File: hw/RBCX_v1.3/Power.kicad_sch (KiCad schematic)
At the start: 42 parts

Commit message: Work in progress
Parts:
- removed J? (x3): Conn_02x04_Counter_Clockwise, Connector_PinHeader_2.54mm:PinHeader_2x04_P2.54mm_Vertical, symbol Connector_Generic:Conn_02x04_Counter_Clockwise
- removed LED? (x6): red, LED_SMD:LED_0603_1608Metric, symbol RBCX-eagle-import:LEDCHIPLED_0603
- removed TP? (x2): TP_06MM, RBCX:TP_06MM, symbol RBCX-eagle-import:TP_06MM
- added D27, D28, D29, D30, D31, D32, D47, D48: red, LED_SMD:LED_0603_1608Metric, symbol Device:LED
- added J2, J3, J4: Conn_02x04_Odd_Even, Connector_PinHeader_2.54mm:PinHeader_2x04_P2.54mm_Vertical, symbol Connector_Generic:Conn_02x04_Odd_Even
- added R181, R182: 1k, Resistor_SMD:R_0201_0603Metric, symbol Device:R
- added TP59, TP8: TP_06MM, RBCX:TP_06MM, symbol RBCX-eagle-import:TP_06MM
- gave numbers to parts that had none: 30
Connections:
- net 3V3: now also D31.2 (A), D32.2 (A), D47.2 (A), D48.2 (A), J2.1 (Pin_1), J2.3 (Pin_3), J2.5 (Pin_5), J2.7 (Pin_7), TP59.P$1 (TP)
- net 5V: now also D29.2 (A), D30.2 (A), J3.1 (Pin_1), J3.3 (Pin_3), J3.5 (Pin_5), J3.7 (Pin_7), TP8.P$1 (TP)
- net GND: now also J2.2 (Pin_2), J2.4 (Pin_4), J2.6 (Pin_6), J2.8 (Pin_8), J3.2 (Pin_2), J3.4 (Pin_4), J3.6 (Pin_6), J3.8 (Pin_8), J4.2 (Pin_2), J4.4 (Pin_4), J4.6 (Pin_6), J4.8 (Pin_8), R181.1, R182.1
- net IN: now also D27.2 (A), D28.2 (A), J4.1 (Pin_1), J4.3 (Pin_3), J4.5 (Pin_5), J4.7 (Pin_7)
- net at R14.1: now also D29.1 (K)
- net at R16.2: now also D31.1 (K)
- net at R10.1, R11.1, R9.1: now also U1.4 (FB); no longer U1. (FB)
- net at R13.2: now also D28.1 (K)
- net at R12.2: now also D27.1 (K)
- net at R15.1: now also D30.1 (K)
- net at R17.2: now also D32.1 (K)
- new net: D47.1 (K), R181.2
- new net: D48.1 (K), R182.2
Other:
- moved on the sheet: TP1, TP2

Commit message: New PCB layout
some changes of schema:
- change PD sink AO33772 to AO33771
- remove power switch
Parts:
- J2, J3, J4: footprint Connector_PinHeader_2.54mm:PinHeader_2x04_P2.54mm_Vertical -> RBCX:PinHeader_2x04_P2.54mm_Vertical
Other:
- sheet Battery Manager ports: added CC1, CC2; removed none
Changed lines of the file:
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@@
+    (stroke (width 0) (type default) (color 0 0 0 0))
+  )
+  (wire (pts (xy 170.18 50.8) (xy 170.18 53.34))
     (stroke (width 0) (type default) (color 0 0 0 0))
   )
@@
     (effects (font (size 1.27 1.27)) (justify left))
   )
-  (hierarchical_label "GND" (shape input) (at 69.85 74.93 0)
+  (hierarchical_label "GND" (shape input) (at 69.85 81.28 0)
     (effects (font (size 1.27 1.27)) (justify left))
   )
@@
     (effects (font (size 1.27 1.27)) (justify right))
   )
+  (hierarchical_label "CC1" (shape bidirectional) (at 69.85 74.93 0)
+    (effects (font (size 1.27 1.27)) (justify left))
+  )
   (hierarchical_label "SDA" (shape bidirectional) (at 69.85 64.77 0)
     (effects (font (size 1.27 1.27)) (justify left))
@@
   (hierarchical_label "GND" (shape input) (at 91.44 180.34 270)
     (effects (font (size 1.27 1.27)) (justify right))
+  )
+  (hierarchical_label "CC2" (shape bidirectional) (at 69.85 77.47 0)
+    (effects (font (size 1.27 1.27)) (justify left))
   )
   (hierarchical_label "GND" (shape input) (at 271.78 128.27 270)
@@
     (property "Reference" "J2" (id 0) (at 260.35 88.9 0))
     (property "Value" "Conn_02x04_Odd_Even" (id 1) (at 260.35 91.44 0))
-    (property "Footprint" "Connector_PinHeader_2.54mm:PinHeader_2x04_P2.54mm_Vertical" (id 2) (at 259.08 97.79 0)
+    (property "Footprint" "RBCX:PinHeader_2x04_P2.54mm_Vertical" (id 2) (at 259.08 97.79 0)
       (effects (font (size 1.27 1.27)) hide)
     )
@@
     (pin "2")
   )
+  (symbol (lib_id "power:PWR_FLAG") (at 170.18 50.8 0) (unit 1)
+    (in_bom yes) (on_board yes) (fields_autoplaced)
+    (property "Reference" "#FLG0102" (id 0) (at 170.18 48.895 0)
+      (effects (font (size 1.27 1.27)) hide)
+    )
+    (property "Value" "PWR_FLAG" (id 1) (at 170.18 45.72 0))
+    (property "Footprint" "" (id 2) (at 170.18 50.8 0)
+      (effects (font (size 1.27 1.27)) hide)
+    )
+    (property "Datasheet" "~" (id 3) (at 170.18 50.8 0)
+      (effects (font (size 1.27 1.27)) hide)
+    )
+    (pin "1")
+  )
   (symbol (lib_id "Device:R") (at 73.66 170.18 180) (unit 1)
     (in_bom yes) (on_board yes)
@@
     (property "Reference" "J4" (id 0) (at 260.35 133.35 0))
     (property "Value" "Conn_02x04_Odd_Even" (id 1) (at 260.35 135.89 0))
-    (property "Footprint" "Connector_PinHeader_2.54mm:PinHeader_2x04_P2.54mm_Vertical" (id 2) (at 259.08 142.24 0)
+    (property "Footprint" "RBCX:PinHeader_2x04_P2.54mm_Vertical" (id 2) (at 259.08 142.24 0)
       (effects (font (size 1.27 1.27)) hide)
     )
@@
     (property "Reference" "J3" (id 0) (at 260.35 111.76 0))
     (property "Value" "Conn_02x04_Odd_Even" (id 1) (at 260.35 114.3 0))
-    (property "Footprint" "Connector_PinHeader_2.54mm:PinHeader_2x04_P2.54mm_Vertical" (id 2) (at 259.08 120.65 0)
+    (property "Footprint" "RBCX:PinHeader_2x04_P2.54mm_Vertical" (id 2) (at 259.08 120.65 0)
       (effects (font (size 1.27 1.27)) hide)
     )
@@
     (pin "2")
   )
-  (sheet (at 38.1 38.1) (size 31.75 38.1) (fields_autoplaced)
+  (sheet (at 38.1 38.1) (size 31.75 44.45) (fields_autoplaced)
     (stroke (width 0.1524) (type solid) (color 0 0 0 0))
     (fill (color 0 0 0 0.0000))
@@
       (effects (font (size 1.27 1.27)) (justify left bottom))
     )
-    (property "Sheet file" "Battery_manager.kicad_sch" (id 1) (at 38.1 76.7846 0)
+    (property "Sheet file" "Battery_manager.kicad_sch" (id 1) (at 38.1 83.1346 0)
       (effects (font (size 1.27 1.27)) (justify left top))
     )
-    (pin "GND" input (at 69.85 74.93 0)
+    (pin "GND" input (at 69.85 81.28 0)
       (effects (font (size 1.27 1.27)) (justify right))
     )
@@
       (effects (font (size 1.27 1.27)) (justify right))
     )
+    (pin "CC1" bidirectional (at 69.85 74.93 0)
+      (effects (font (size 1.27 1.27)) (justify right))
+    )
+    (pin "CC2" bidirectional (at 69.85 77.47 0)
+      (effects (font (size 1.27 1.27)) (justify right))
+    )

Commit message: Production files
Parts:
- BAT1: JLCPCB_CORRECTION (none) -> 0;0;180
- J2, J3, J4: JLCPCB_CORRECTION (none) -> 1.27;-3.81;90; LCSC C225289 -> C124386
- TP1, TP2, TP4, TP5, TP59, TP6, TP7, TP8, X1: JLCPCB_IGNORE (none) -> 1
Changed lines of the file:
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@@
       (effects (font (size 1.27 1.27)) hide)
     )
-    (property "LCSC" "C225289" (id 4) (at 259.08 97.79 0)
+    (property "LCSC" "C124386" (id 4) (at 259.08 97.79 0)
       (effects (font (size 1.27 1.27)) hide)
     )
     (property "Basic/Extended" "E" (id 5) (at 259.08 97.79 0)
+      (effects (font (size 1.27 1.27)) hide)
+    )
+    (property "JLCPCB_CORRECTION" "1.27;-3.81;90" (id 6) (at 259.08 97.79 0)
       (effects (font (size 1.27 1.27)) hide)
     )
@@
       (effects (font (size 1.27 1.27)) hide)
     )
+    (property "JLCPCB_IGNORE" "1" (id 4) (at 255.397 35.56 0)
+      (effects (font (size 1.27 1.27)) hide)
+    )
     (pin "P$1")
   )
@@
       (effects (font (size 1.27 1.27)) hide)
     )
-    (property "LCSC" "C225289" (id 4) (at 259.08 142.24 0)
+    (property "LCSC" "C124386" (id 4) (at 259.08 142.24 0)
       (effects (font (size 1.27 1.27)) hide)
     )
     (property "Basic/Extended" "E" (id 5) (at 259.08 142.24 0)
+      (effects (font (size 1.27 1.27)) hide)
+    )
+    (property "JLCPCB_CORRECTION" "1.27;-3.81;90" (id 6) (at 259.08 142.24 0)
       (effects (font (size 1.27 1.27)) hide)
     )
@@
       (effects (font (size 1.27 1.27)) hide)
     )
-    (property "LCSC" "C225289" (id 4) (at 259.08 120.65 0)
+    (property "LCSC" "C124386" (id 4) (at 259.08 120.65 0)
       (effects (font (size 1.27 1.27)) hide)
     )
     (property "Basic/Extended" "E" (id 5) (at 259.08 120.65 0)
+      (effects (font (size 1.27 1.27)) hide)
+    )
+    (property "JLCPCB_CORRECTION" "1.27;-3.81;90" (id 6) (at 259.08 120.65 0)
       (effects (font (size 1.27 1.27)) hide)
     )
@@
       (effects (font (size 1.27 1.27)) hide)
     )
+    (property "JLCPCB_CORRECTION" "0;0;180" (id 6) (at 50.8 119.38 0)
+      (effects (font (size 1.27 1.27)) hide)
+    )
     (pin "1")
     (pin "2")
@@
       (effects (font (size 1.27 1.27)) hide)
     )
+    (property "JLCPCB_IGNORE" "1" (id 4) (at 147.32 114.3 0)
+      (effects (font (size 1.27 1.27)) hide)
+    )
     (pin "P$1")
   )
@@
       (effects (font (size 1.27 1.27)) hide)
     )
+    (property "JLCPCB_IGNORE" "1" (id 4) (at 265.43 35.56 0)
+      (effects (font (size 1.27 1.27)) hide)
+    )
     (pin "P$1")
   )
@@
     )
     (property "Datasheet" "" (id 3) (at 127 114.3 0)
+      (effects (font (size 1.27 1.27)) hide)
+    )
+    (property "JLCPCB_IGNORE" "1" (id 4) (at 127 114.3 0)
       (effects (font (size 1.27 1.27)) hide)
     )
@@
       (effects (font (size 1.27 1.27)) hide)
     )
+    (property "JLCPCB_IGNORE" "1" (id 4) (at 264.287 59.69 0)
+      (effects (font (size 1.27 1.27)) hide)
+    )
     (pin "1")
     (pin "2")
@@
       (effects (font (size 1.27 1.27)) hide)
     )
+    (property "JLCPCB_IGNORE" "1" (id 4) (at 242.57 35.56 0)
+      (effects (font (size 1.27 1.27)) hide)
+    )
     (pin "P$1")
   )
@@
     )
     (property "Datasheet" "" (id 3) (at 139.7 60.96 0)
+      (effects (font (size 1.27 1.27)) hide)
+    )
+    (property "JLCPCB_IGNORE" "1" (id 4) (at 139.7 60.96 0)
       (effects (font (size 1.27 1.27)) hide)
     )
@@
       (effects (font (size 1.27 1.27)) hide)
     )
+    (property "JLCPCB_IGNORE" "1" (id 4) (at 229.87 35.56 0)
+      (effects (font (size 1.27 1.27)) hide)
+    )
     (pin "P$1")
   )
@@
       (effects (font (size 1.27 1.27)) hide)
     )
+    (property "JLCPCB_IGNORE" "1" (id 4) (at 264.287 54.61 0)
+      (effects (font (size 1.27 1.27)) hide)
+    )
     (pin "1")
     (pin "2")
@@
       (effects (font (size 1.27 1.27)) hide)
     )
+    (property "JLCPCB_IGNORE" "1" (id 4) (at 58.42 99.06 0)
+      (effects (font (size 1.27 1.27)) hide)
+    )

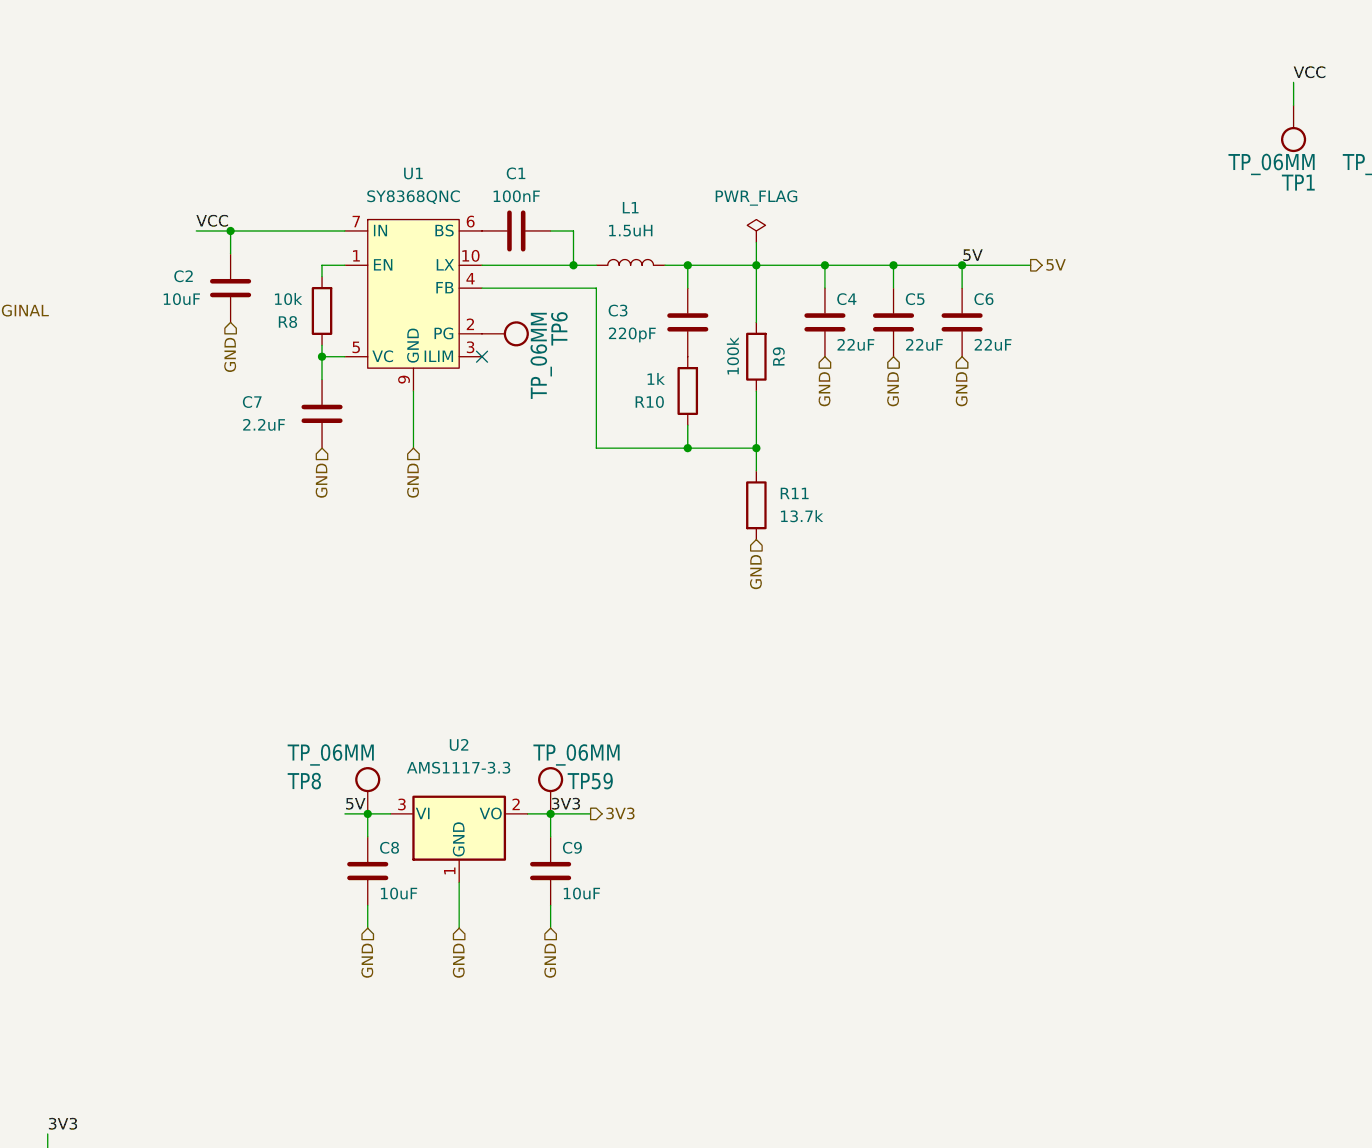
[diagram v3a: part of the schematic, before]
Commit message: Protective resistors for I2C on connectors
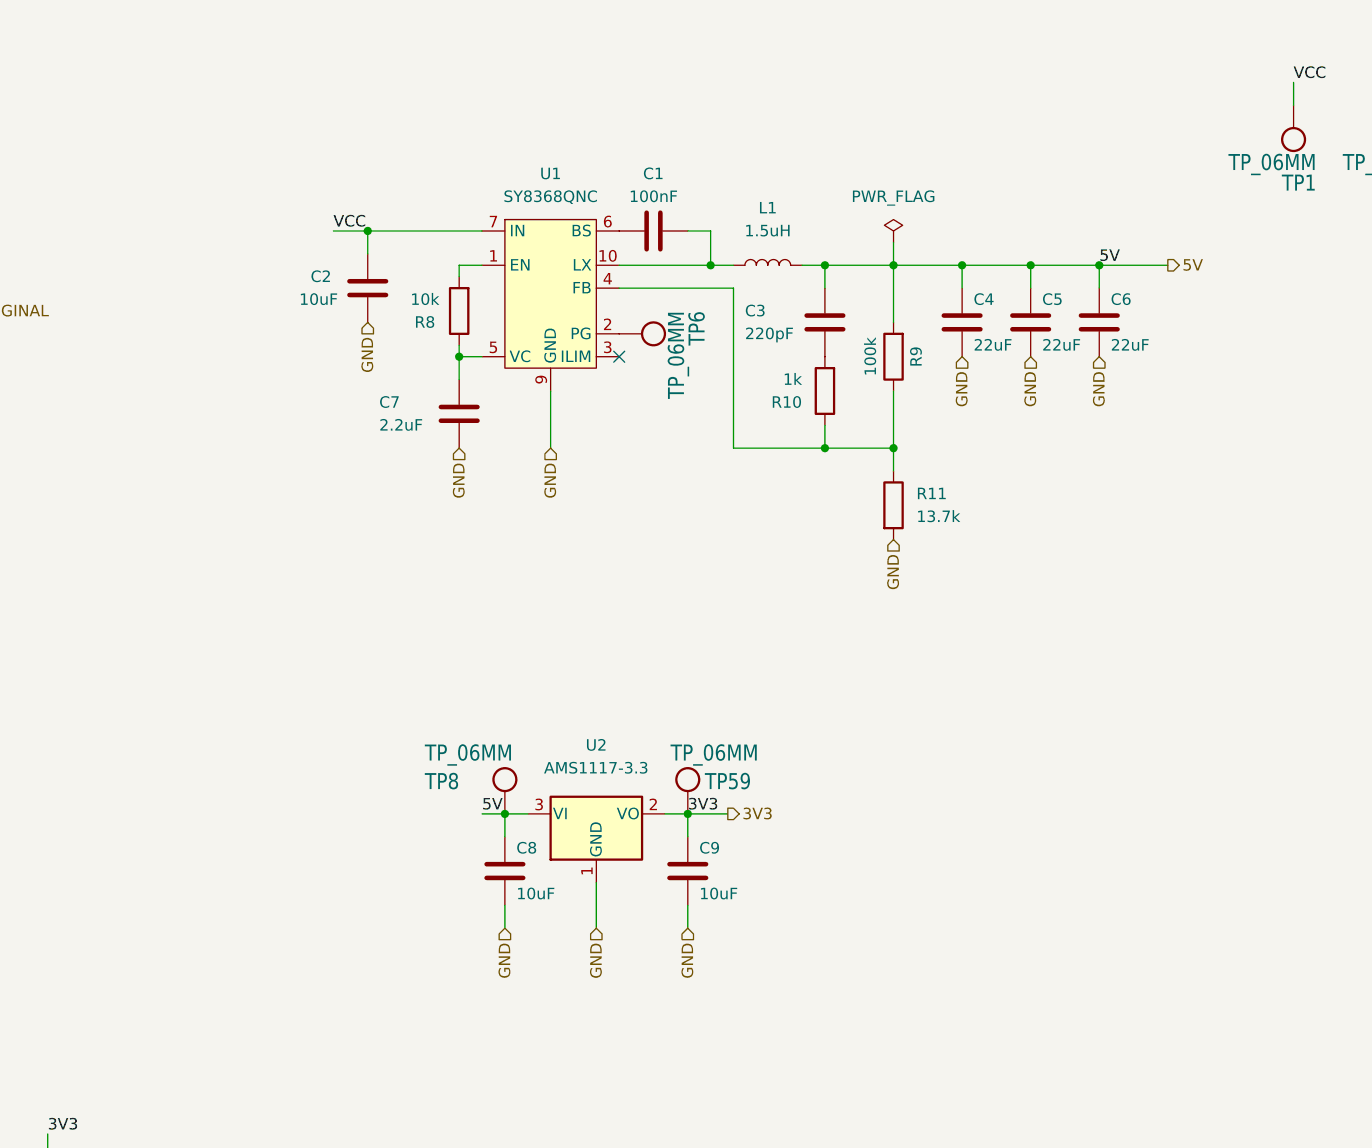
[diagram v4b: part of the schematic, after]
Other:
- moved on the sheet: C1, C2, C3, C4, C5, C6, C7, C8, C9, L1, R10, R11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

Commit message: Kuba issues
Change of power transistor from JSM3622 to JMSL0302AU

NTC connectors

Moving the Cell balancer behind the switch

and some little things
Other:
- sheet Battery Manager ports: added VBUS_CS; removed CC1, CC2
- moved on the sheet: C1, C2, C3, C4, C5, C6, C7, C8, C9, L1, R10, R11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

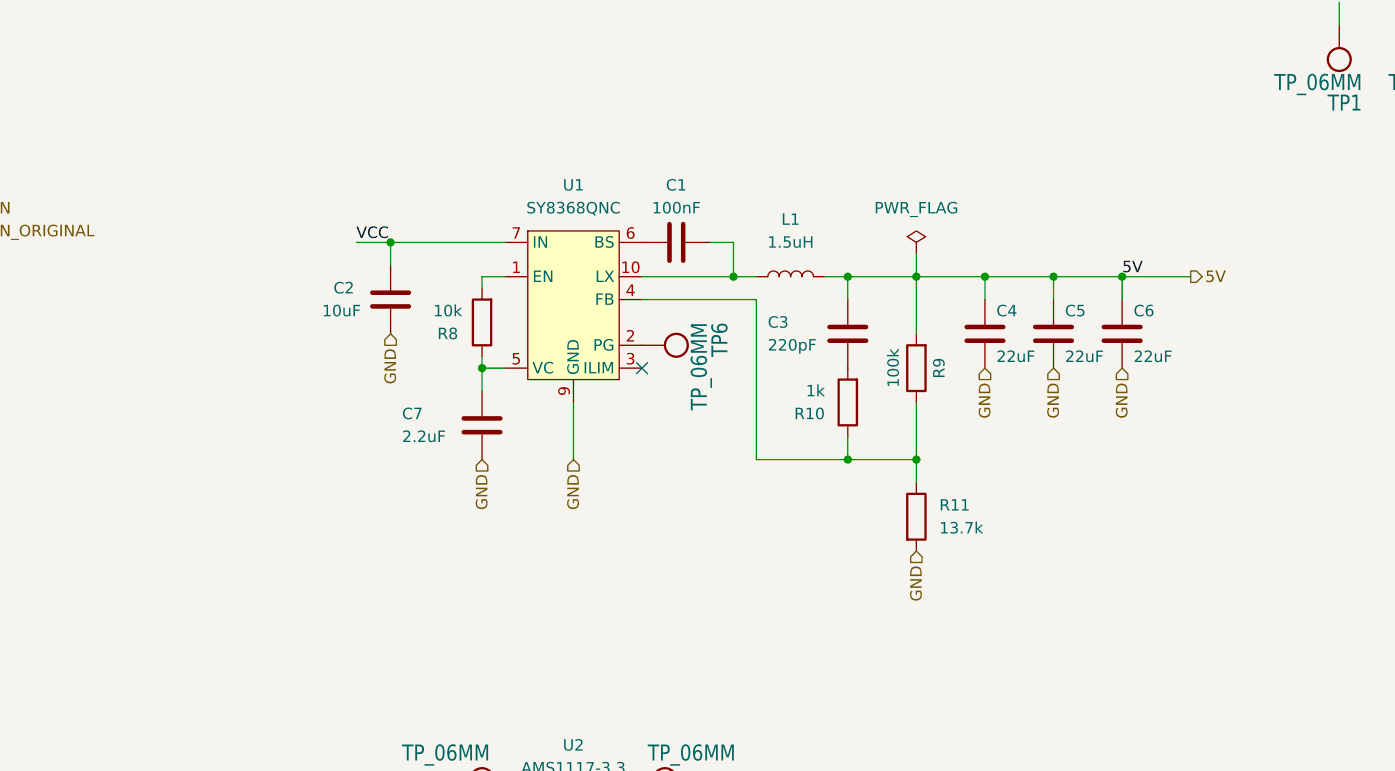
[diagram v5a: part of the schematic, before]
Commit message: USB-DET level shifter
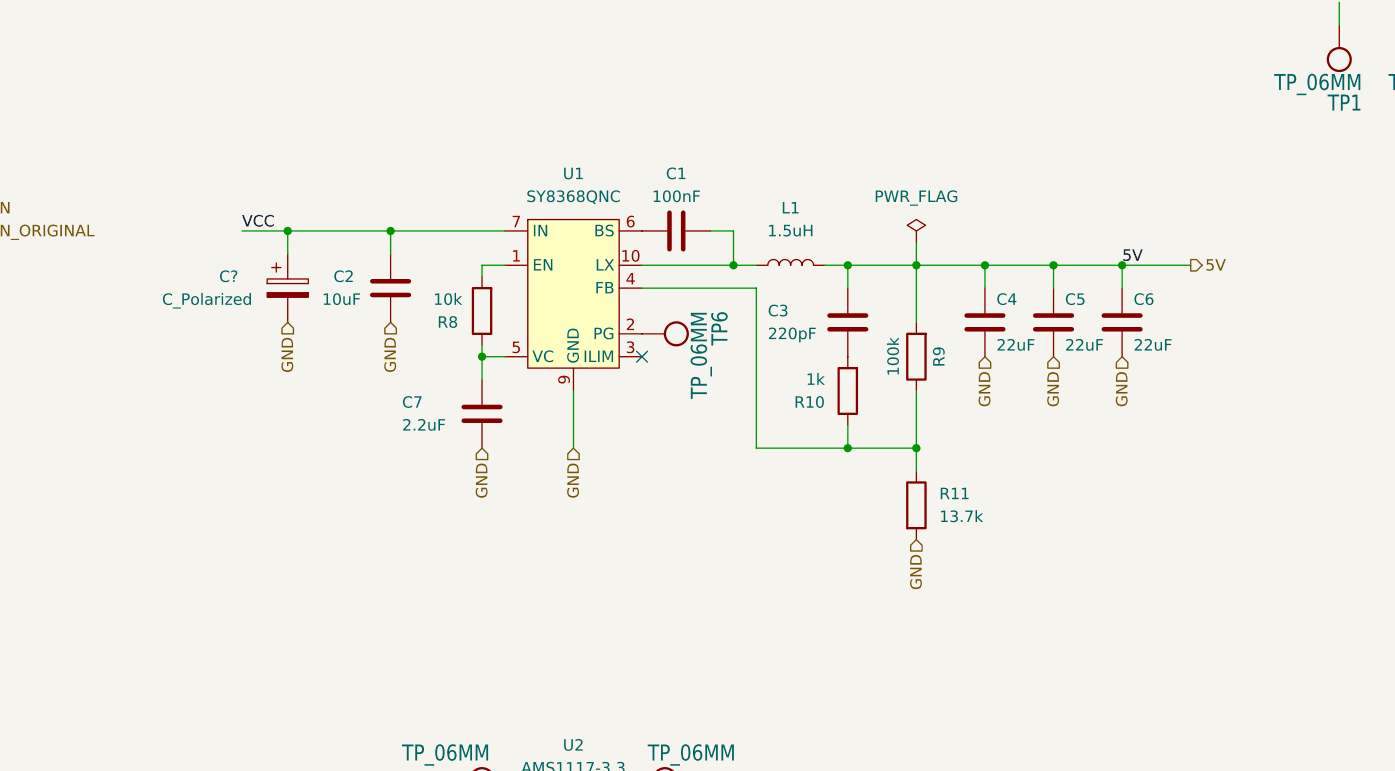
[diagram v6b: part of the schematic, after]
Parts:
- added C?: C_Polarized, Capacitor_SMD:CP_Elec_8x11.9, symbol Device:C_Polarized
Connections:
- net GND: now also C?.2
- net IN: now also C?.1
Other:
- moved on the sheet: C1, C2, C3, C4, C5, C6, C7, L1, R10, R11, R8, R9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

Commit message: WIP
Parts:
- gave numbers to parts that had none: 1
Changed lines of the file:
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@@
   (symbol (lib_id "Device:C_Polarized") (at 113.03 64.77 0) (unit 1)
     (in_bom yes) (on_board yes)
-    (property "Reference" "C?" (id 0) (at 105.41 63.5 0)
+    (property "Reference" "C85" (id 0) (at 105.41 63.5 0)
       (effects (font (size 1.27 1.27)) (justify left))
     )
